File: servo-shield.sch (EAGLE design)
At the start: 7 parts, among them IC1 24AA01P, K1 PIN20X2

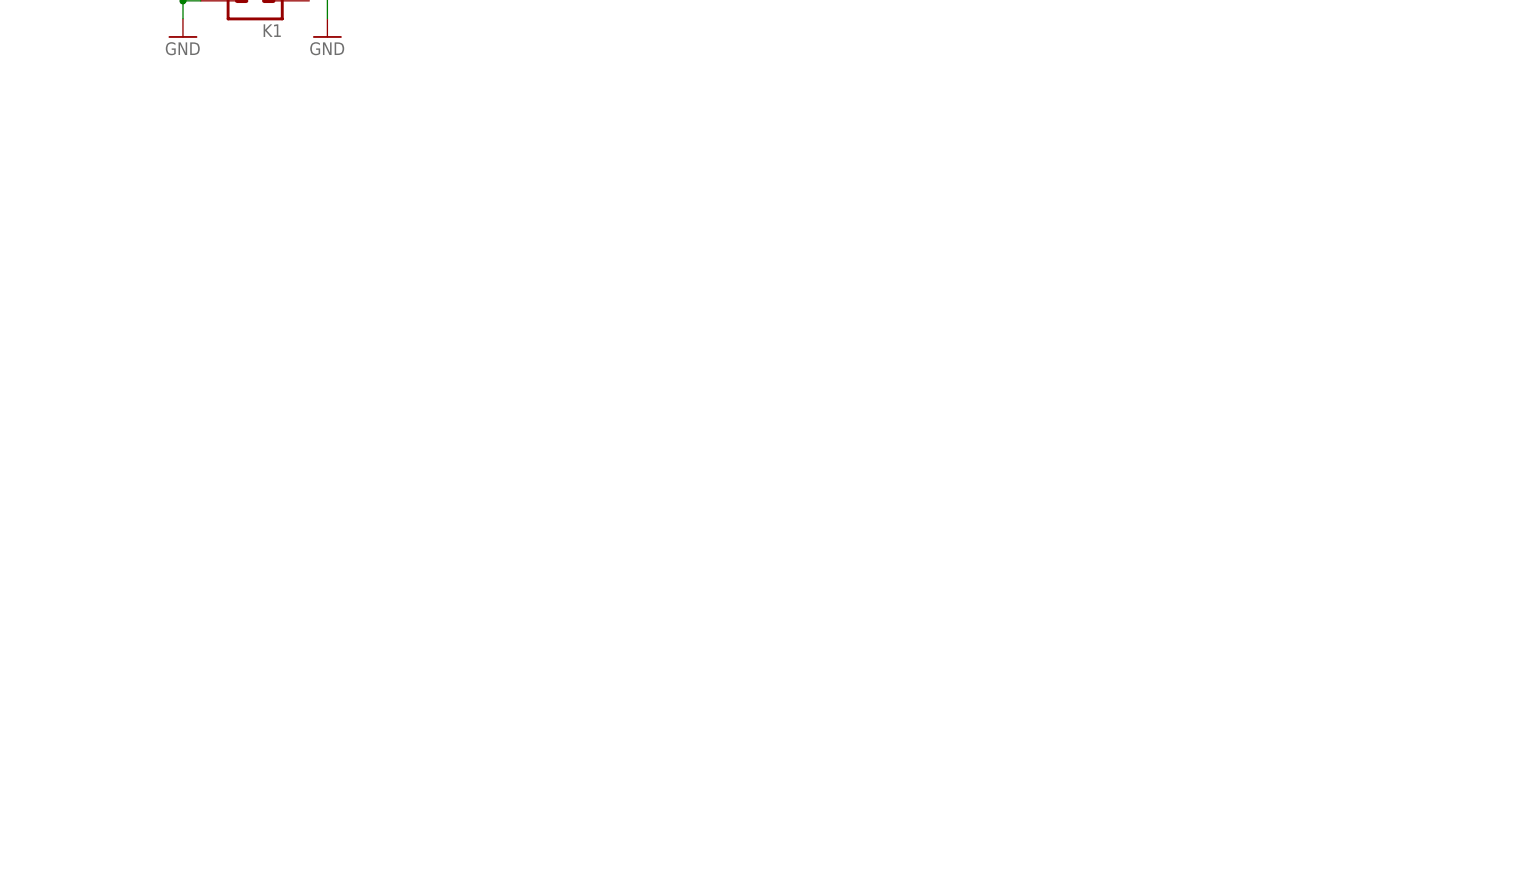
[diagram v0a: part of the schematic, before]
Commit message: Add PCA9685
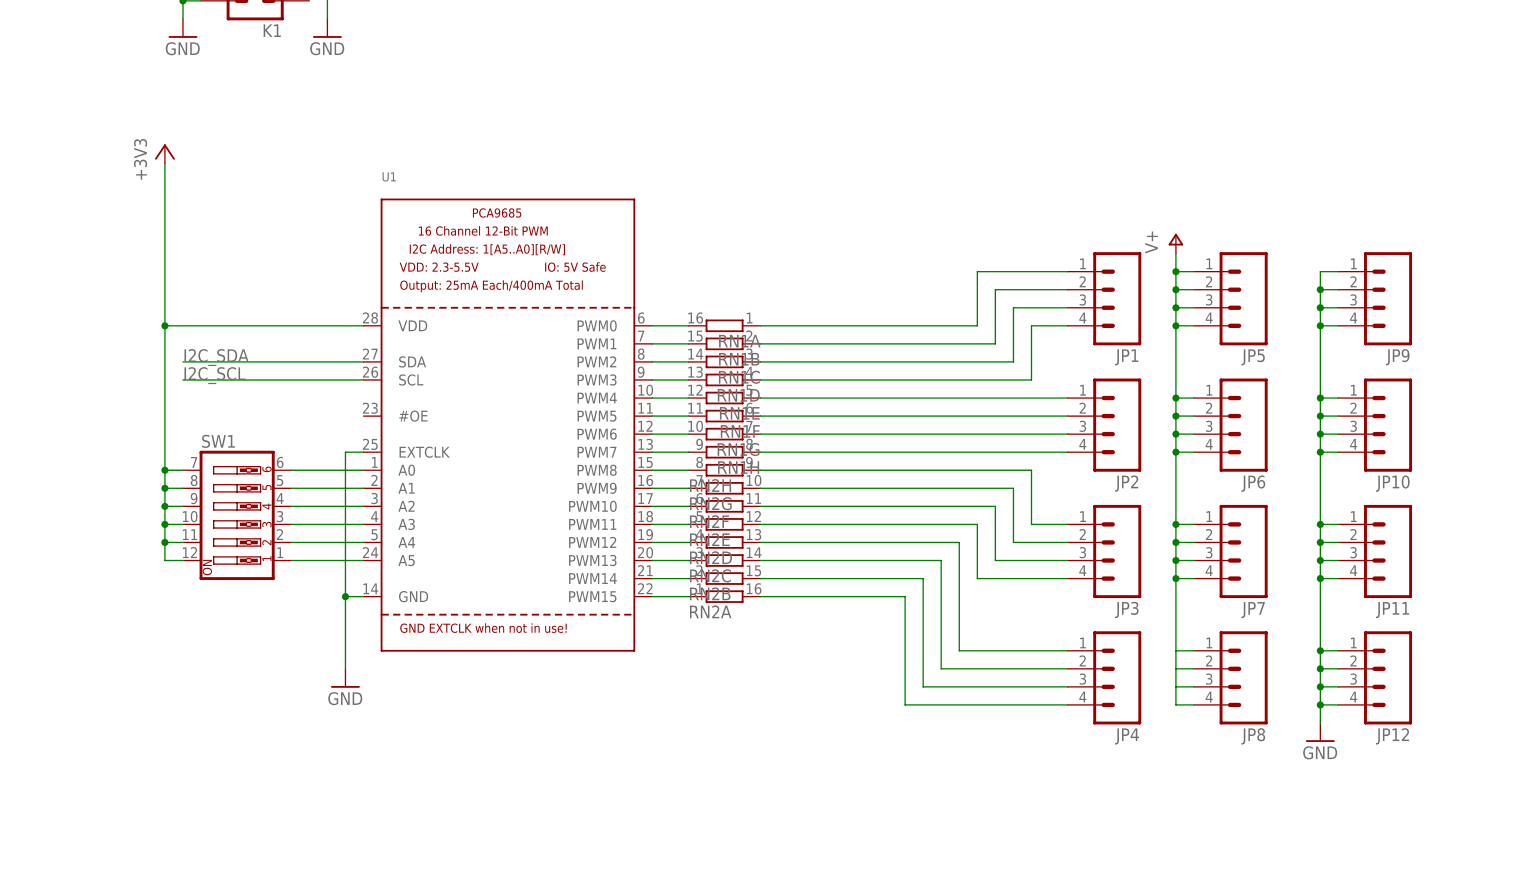
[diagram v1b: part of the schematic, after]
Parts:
- added JP1, JP10, JP11, JP12, JP2, JP3, JP4, JP5, JP6, JP7, JP8, JP9: (no value), SparkFun-Connectors:M04LOCK
- added RN1, RN2: (no value), resistor-dil:8R-N
- added SW1: (no value), special:SW_DIP-6
- added U1: (no value), adafruit:PCA9685
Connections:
- new net I2C_SCL: U1.SCL
- new net I2C_SDA: U1.SDA
- new net N$1: RN2G.1, U1.PWM9
- new net N$10: JP3.2, RN2G.2
- new net N$11: SW1.1, U1.A5
- new net N$12: SW1.2, U1.A4
- new net N$13: SW1.3, U1.A3
- new net N$14: SW1.4, U1.A2
- new net N$15: SW1.5, U1.A1
- new net N$16: SW1.6, U1.A0
- new net N$17: JP3.3, RN2F.2
- new net N$18: JP3.4, RN2E.2
- new net N$19: JP4.1, RN2D.2
- new net N$2: RN2H.1, U1.PWM8
- new net N$20: JP4.2, RN2C.2
- new net N$21: JP4.3, RN2B.2
- new net N$22: JP4.4, RN2A.2
- new net N$23: RN2A.1, U1.PWM15
- new net N$24: RN2B.1, U1.PWM14
- new net N$25: RN2C.1, U1.PWM13
- new net N$26: RN2D.1, U1.PWM12
- new net N$27: RN2E.1, U1.PWM11
- new net N$28: RN2F.1, U1.PWM10
- new net N$29: RN1G.2, U1.PWM6
- new net N$3: RN1H.2, U1.PWM7
- new net N$30: RN1F.2, U1.PWM5
- new net N$31: RN1E.2, U1.PWM4
- new net N$32: RN1D.2, U1.PWM3
- new net N$33: RN1C.2, U1.PWM2
- new net N$34: RN1B.2, U1.PWM1
- new net N$35: RN1A.2, U1.PWM0
- new net N$36: JP2.1, RN1E.1
- new net N$37: JP2.4, RN1H.1
- new net N$38: JP2.3, RN1G.1
- new net N$39: JP2.2, RN1F.1
- new net N$5: JP1.4, RN1D.1
- new net N$6: JP1.3, RN1C.1
- new net N$7: JP1.2, RN1B.1
- new net N$8: JP1.1, RN1A.1
- new net N$9: JP3.1, RN2H.2
- new net V+: JP5.1, JP5.2, JP5.3, JP5.4, JP6.1, JP6.2, JP6.3, JP6.4, JP7.1, JP7.2, JP7.3, JP7.4, JP8.1, JP8.2, JP8.3, JP8.4
- net +3V3: now also SW1.10, SW1.11, SW1.12, SW1.7, SW1.8, SW1.9, U1.VDD
- net GND: now also JP10.1, JP10.2, JP10.3, JP10.4, JP11.1, JP11.2, JP11.3, JP11.4, JP12.1, JP12.2, JP12.3, JP12.4, JP9.1, JP9.2, JP9.3, JP9.4, U1.EXTCLK, U1.GND

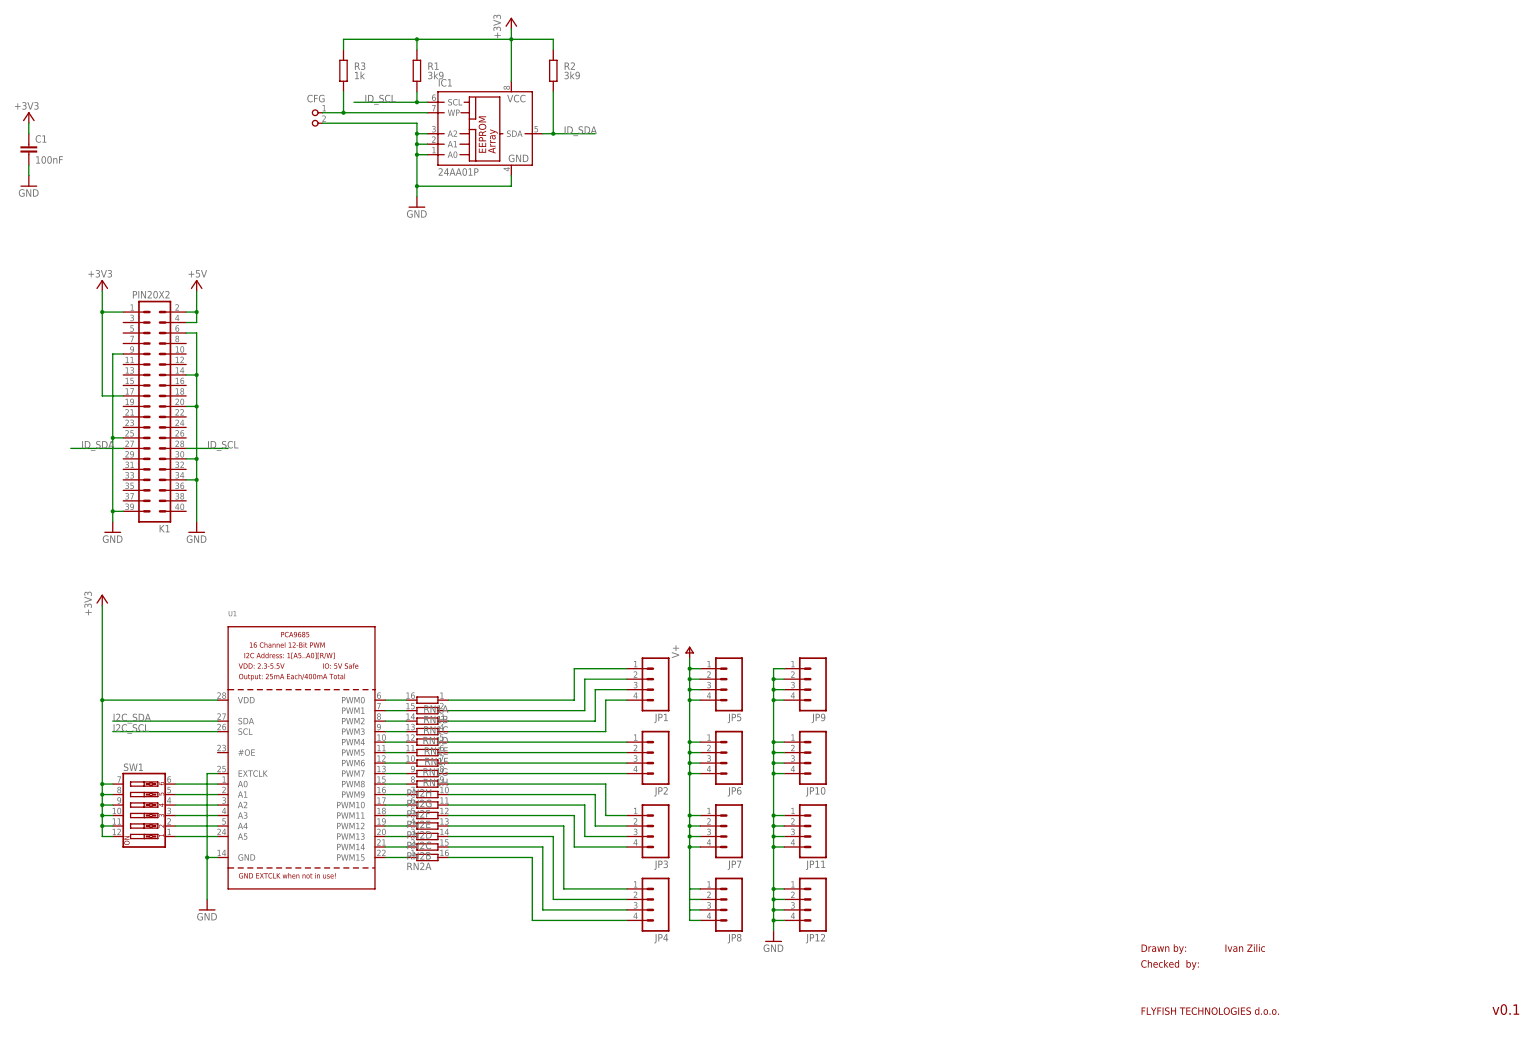
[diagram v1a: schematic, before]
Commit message: Finished current schematic.. Must add power supply and power regulation
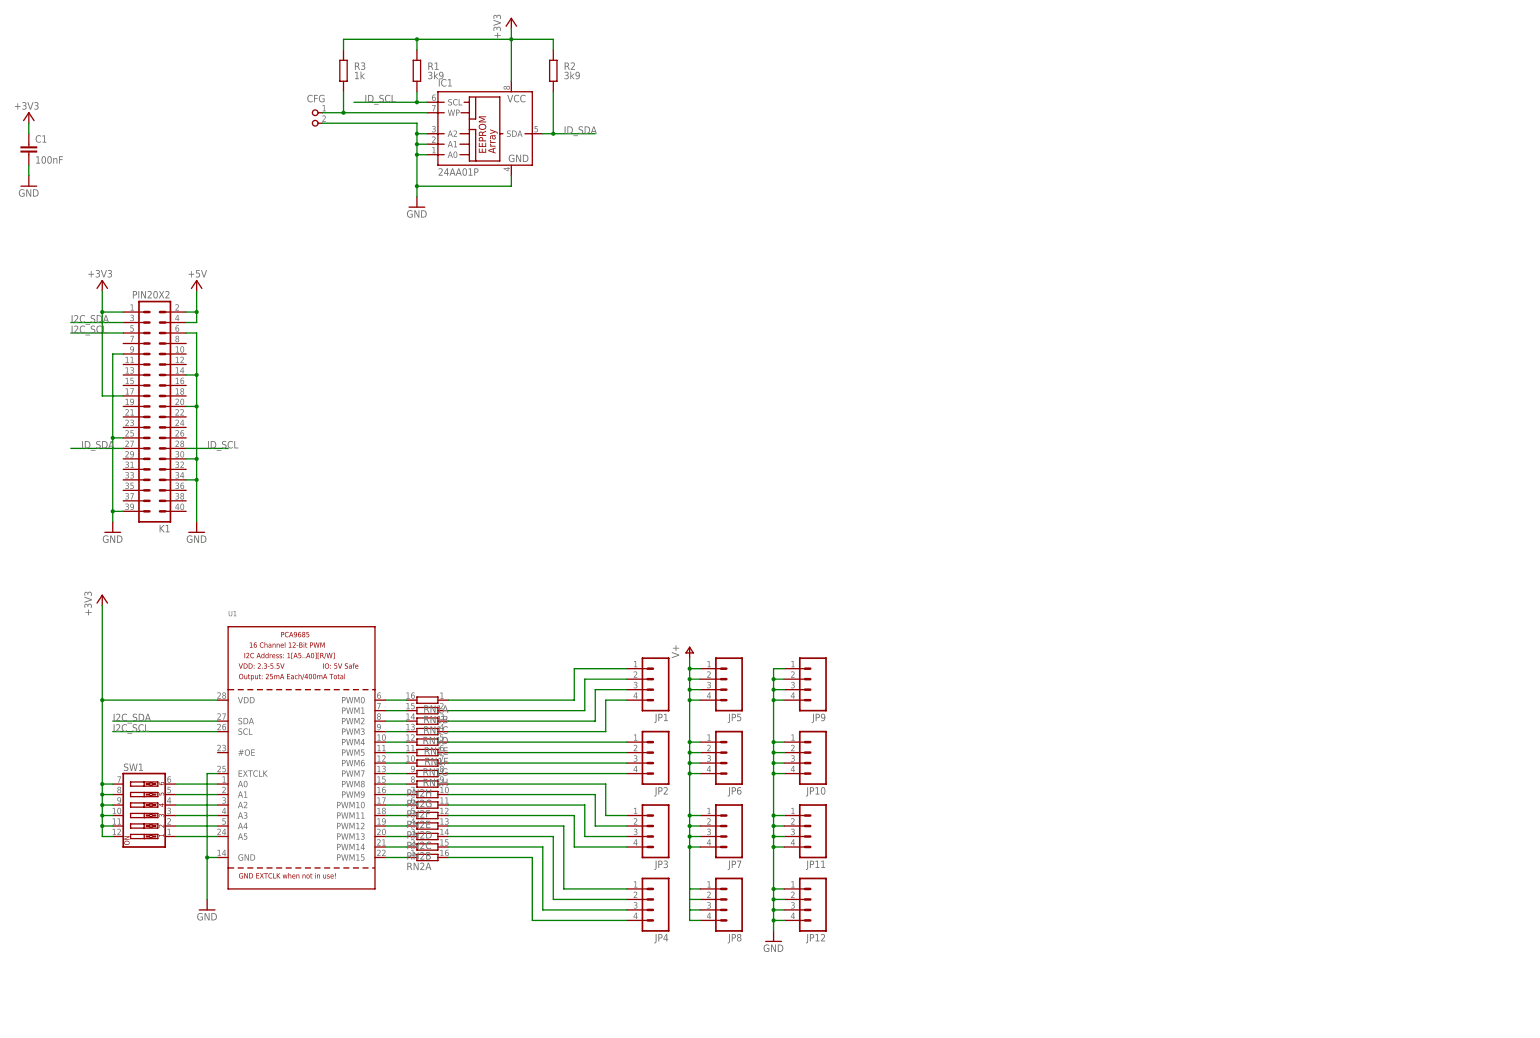
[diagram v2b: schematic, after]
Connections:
- net I2C_SCL: now also K1.5
- net I2C_SDA: now also K1.3
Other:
- note removed: "Checked by:"
- note removed: "Drawn by:"
- note removed: "FLYFISH TECHNOLOGIES d.o.o."
- note removed: "Ivan Zilic"
- note removed: "v0.1"
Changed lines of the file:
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@@
 <parts>
 <part name="K1" library="FLYFISH" deviceset="PIN20X2" device=""/>
-<part name="FRAME1" library="frames" deviceset="A3L-LOC" device=""/>
 <part name="GND10" library="supply1" deviceset="GND" device=""/>
 <part name="R1" library="rcl" deviceset="R-EU_" device="0204/7" value="3k9">
@@
 <sheet>
 <plain>
-<text x="289.56" y="20.32" size="1.778" layer="94" ratio="15">Drawn by:</text>
-<text x="289.56" y="16.51" size="1.778" layer="94" ratio="15">Checked  by:</text>
-<text x="289.56" y="5.08" size="1.778" layer="94">FLYFISH TECHNOLOGIES d.o.o.</text>
-<text x="309.88" y="20.32" size="1.778" layer="94">Ivan Zilic</text>
-<text x="374.65" y="5.08" size="2.54" layer="94" ratio="10">v0.1</text>
 </plain>
 <instances>
 <instance part="K1" gate="G$1" x="50.8" y="152.4" rot="R180"/>
-<instance part="FRAME1" gate="G$1" x="0" y="0"/>
 <instance part="GND10" gate="1" x="60.96" y="121.92"/>
 <instance part="R1" gate="G$1" x="114.3" y="233.68" smashed="yes" rot="R90">
@@
 <label x="40.64" y="76.2" size="1.778" layer="95"/>
 </segment>
+<segment>
+<pinref part="K1" gate="G$1" pin="3"/>
+<wire x1="43.18" y1="172.72" x2="30.48" y2="172.72" width="0.1524" layer="91"/>
+<label x="30.48" y="172.72" size="1.778" layer="95"/>
+</segment>
 </net>
 <net name="I2C_SCL" class="0">
@@
 <label x="40.64" y="73.66" size="1.778" layer="95"/>
 </segment>
-</net>
+<segment>
+<pinref part="K1" gate="G$1" pin="5"/>
+<wire x1="43.18" y1="170.18" x2="30.48" y2="170.18" width="0.1524" layer="91"/>
+<label x="30.48" y="170.18" size="1.778" layer="95"/>
+</segment>
+</net>
